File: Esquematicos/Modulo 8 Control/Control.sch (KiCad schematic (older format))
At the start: 6 parts

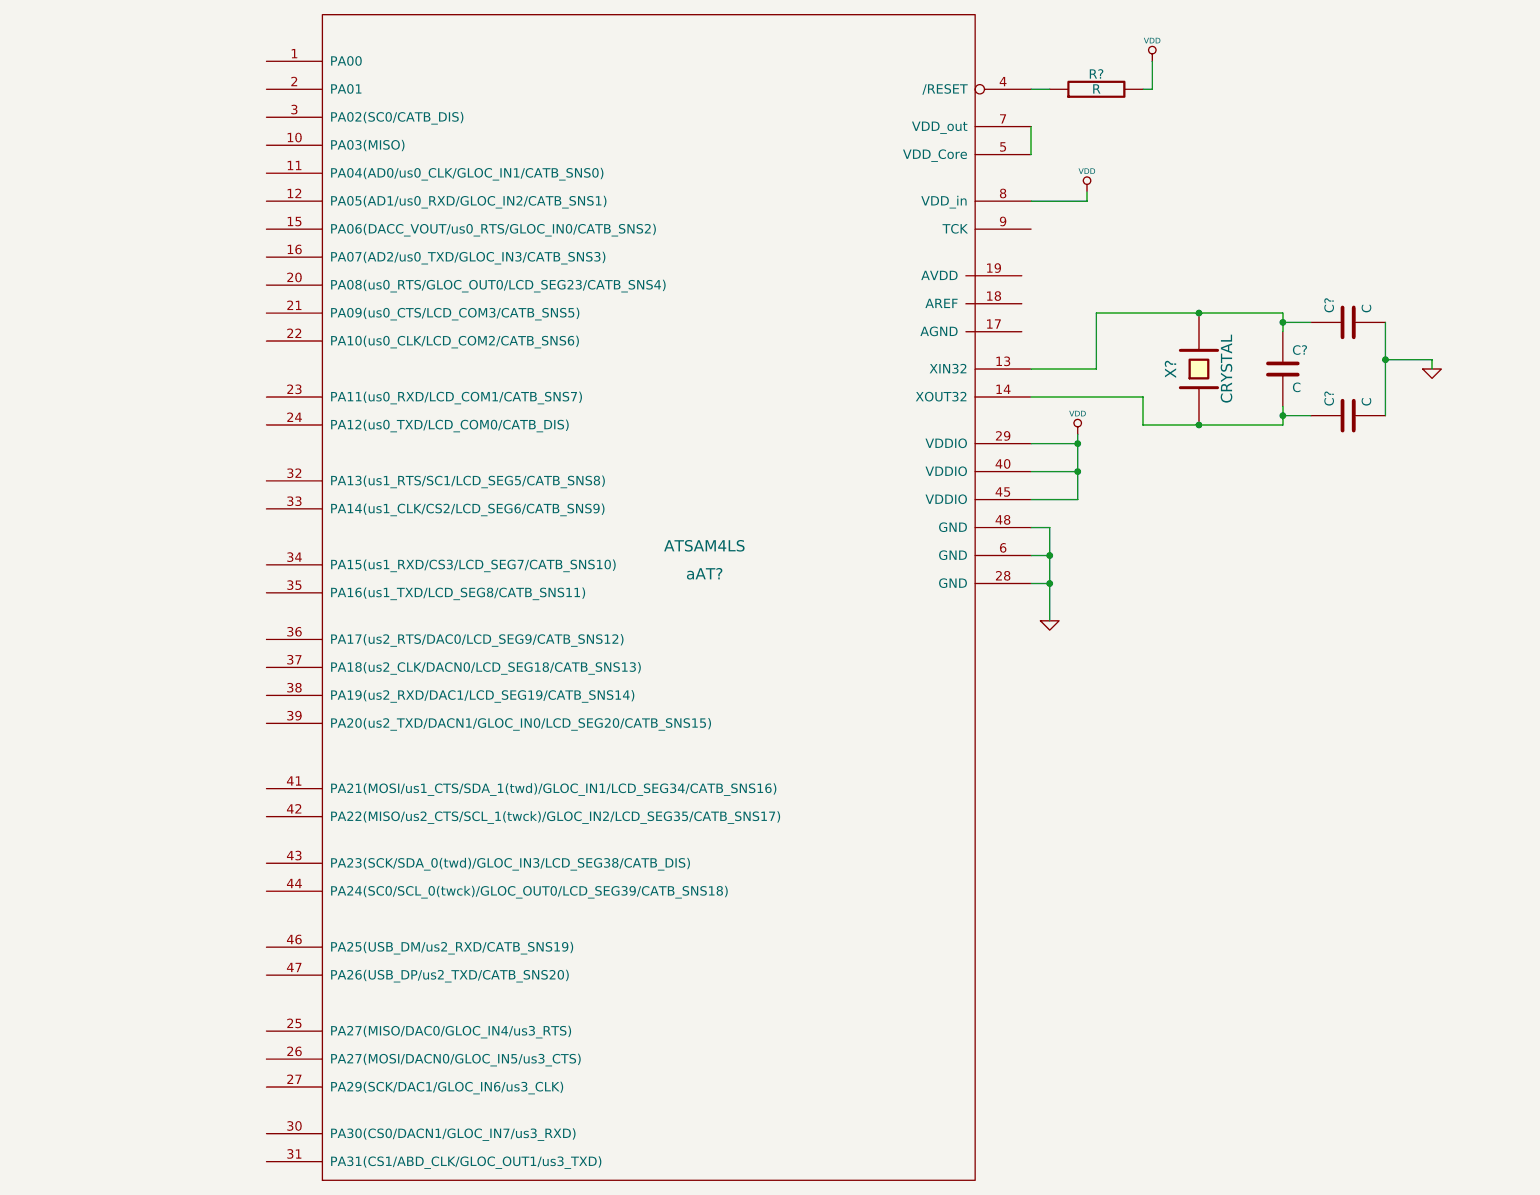
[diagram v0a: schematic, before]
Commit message: actualizacion mod 8 y 12
esch mod8 mejorado, versión 2 del mod 12
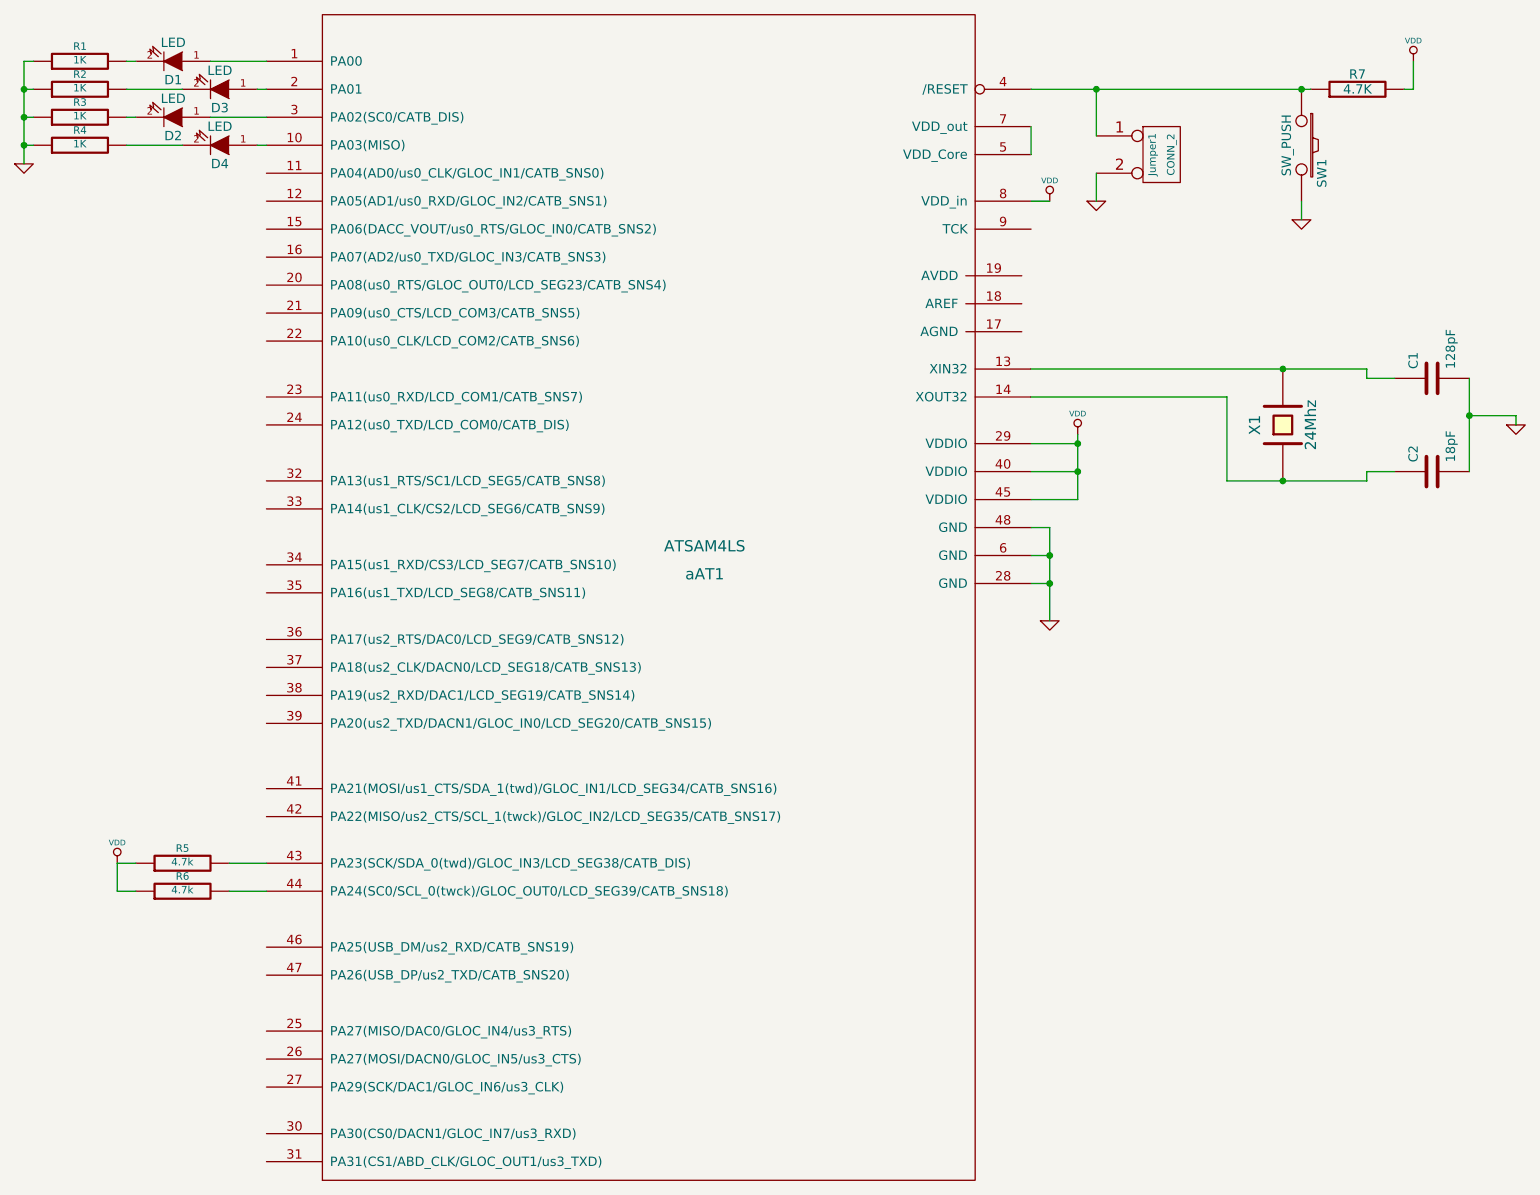
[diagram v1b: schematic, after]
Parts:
- removed C?: C, symbol C
- added D1, D2, D3, D4: LED, ~, symbol LED
- added Jumper1: CONN_2, symbol CONN_2
- added R1, R2, R3, R4: 1K, ~, symbol R
- added R5, R6: 4.7k, ~, symbol R
- added SW1: SW_PUSH, ~, symbol SW_PUSH
- C1: renamed from C?; value C -> 128pF
- C2: renamed from C?; value C -> 18pF
- R7: renamed from R?; value R -> 4.7K
- X1: renamed from X?; value CRYSTAL -> 24Mhz
- gave numbers to parts that had none: 1
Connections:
- net GND: now also Jumper1.2 (PM), R1.1, R2.1, R3.1, R4.1, SW1.2
- net VDD: now also R5.1, R6.1
- net at aAT1.1 (PA00): now also D1.1 (A)
- net at aAT1.10 (PA03(MISO)): now also D4.1 (A)
- net at aAT1.2 (PA01): now also D3.1 (A)
- net at aAT1.3 (PA02(SC0/CATB_DIS)): now also D2.1 (A)
- net at R7.1, aAT1.4 (/RESET): now also Jumper1.1 (P1), SW1.1
- net at aAT1.43 (PA23(SCK/SDA_0(twd)/GLOC_IN3/LCD_SEG38/CATB_DIS)): now also R5.2
- net at aAT1.44 (PA24(SC0/SCL_0(twck)/GLOC_OUT0/LCD_SEG39/CATB_SNS18)): now also R6.2
- new net: D1.2 (K), R1.2
- new net: D3.2 (K), R2.2
- new net: D2.2 (K), R3.2
- new net: D4.2 (K), R4.2
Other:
- moved on the sheet: C1, C2, R7, X1
